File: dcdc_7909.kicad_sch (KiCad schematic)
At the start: 46 parts, among them J1 V_IN, J2 G_IN, J3 RFShield_OnePiece, J4 +10V, J5 G_OUT, J6 -10V, U1 LT3471, U2 LT3045xMSE, U3 LT3094xMSE

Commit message: V2 PCB almost finished.
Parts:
- added C1: 22u, Capacitor_SMD:C_0805_2012Metric_Pad1.18x1.45mm_HandSolder, symbol Device:C_Small
- C10: renamed from C9; footprint Capacitor_SMD:C_1206_3216Metric_Pad1.42x1.75mm_HandSolder -> Capacitor_SMD:C_0805_2012Metric_Pad1.18x1.45mm_HandSolder; LCSC (none) -> C45783
- C11: renamed from C10; footprint Capacitor_SMD:C_0603_1608Metric_Pad1.08x0.95mm_HandSolder -> Capacitor_SMD:C_0603_1608Metric; LCSC (none) -> C57112
- C12: renamed from C11; footprint Capacitor_SMD:C_1206_3216Metric_Pad1.42x1.75mm_HandSolder -> Capacitor_SMD:C_0805_2012Metric_Pad1.18x1.45mm_HandSolder; LCSC (none) -> C15850
- C13: renamed from C12; footprint Capacitor_SMD:C_1206_3216Metric_Pad1.42x1.75mm_HandSolder -> Capacitor_SMD:C_0805_2012Metric_Pad1.18x1.45mm_HandSolder; LCSC (none) -> C15850
- C14: renamed from C13; footprint Capacitor_SMD:C_1206_3216Metric_Pad1.42x1.75mm_HandSolder -> Capacitor_SMD:C_0805_2012Metric_Pad1.18x1.45mm_HandSolder; LCSC (none) -> C15850
- C15: renamed from C14; footprint Capacitor_SMD:C_1206_3216Metric_Pad1.42x1.75mm_HandSolder -> Capacitor_SMD:C_0805_2012Metric_Pad1.18x1.45mm_HandSolder; LCSC (none) -> C15850
- C16: renamed from C15; footprint Capacitor_SMD:C_1206_3216Metric_Pad1.42x1.75mm_HandSolder -> Capacitor_SMD:C_0805_2012Metric_Pad1.18x1.45mm_HandSolder; LCSC (none) -> C15850
- C17: renamed from C16; footprint Capacitor_SMD:C_0603_1608Metric_Pad1.05x0.95mm_HandSolder -> Capacitor_SMD:C_0603_1608Metric; LCSC (none) -> C57112
- C18: renamed from C17; footprint Capacitor_SMD:C_1206_3216Metric_Pad1.42x1.75mm_HandSolder -> Capacitor_SMD:C_0805_2012Metric_Pad1.18x1.45mm_HandSolder; LCSC (none) -> C15850
- C19: renamed from C18; LCSC (none) -> DO NOT POPULATE
- C2: renamed from C1; footprint Capacitor_SMD:C_1206_3216Metric_Pad1.42x1.75mm_HandSolder -> Capacitor_SMD:C_0603_1608Metric; LCSC (none) -> C96446
- C20: renamed from C19; footprint Capacitor_SMD:C_0603_1608Metric_Pad1.05x0.95mm_HandSolder -> Capacitor_SMD:C_0603_1608Metric; LCSC (none) -> C57112
- C21: renamed from C20; LCSC (none) -> DO NOT POPULATE
- C3: renamed from C2; footprint Capacitor_SMD:C_0603_1608Metric_Pad1.08x0.95mm_HandSolder -> Capacitor_SMD:C_0603_1608Metric; LCSC (none) -> C14663
- C4: renamed from C3; footprint Capacitor_SMD:C_0603_1608Metric_Pad1.08x0.95mm_HandSolder -> Capacitor_SMD:C_0603_1608Metric; LCSC (none) -> C1604
- C5: renamed from C4; footprint Capacitor_SMD:C_1206_3216Metric_Pad1.42x1.75mm_HandSolder -> Capacitor_SMD:C_0805_2012Metric_Pad1.18x1.45mm_HandSolder; LCSC (none) -> C45783
- C6: renamed from C5; footprint Capacitor_SMD:C_0603_1608Metric_Pad1.08x0.95mm_HandSolder -> Capacitor_SMD:C_0603_1608Metric; LCSC (none) -> C57112
- C7: renamed from C6; footprint Capacitor_SMD:C_1206_3216Metric_Pad1.42x1.75mm_HandSolder -> Capacitor_SMD:C_0603_1608Metric; LCSC (none) -> C96446
- C8: renamed from C7; footprint Capacitor_SMD:C_1206_3216Metric_Pad1.42x1.75mm_HandSolder -> Capacitor_SMD:C_0603_1608Metric; LCSC (none) -> C96446
- C9: renamed from C8; value 500p -> 470p; footprint Capacitor_SMD:C_0603_1608Metric_Pad1.08x0.95mm_HandSolder -> Capacitor_SMD:C_0603_1608Metric; LCSC (none) -> C1620
- D1, D2: footprint Diode_SMD:D_SOD-323_HandSoldering -> Diode_SMD:D_PowerDI-123; LCSC (none) -> C155287
- D3, D4, J1, J2, J4, J5, J6, TP1, U2, U3: LCSC (none) -> DO NOT POPULATE
- J3: footprint (none) -> RF_Shielding:Laird_Technologies_BMI-S-102_16.50x16.50mm; LCSC (none) -> DO NOT POPULATE
- L1, L2, L3: footprint Inductor_SMD:L_Coilcraft_LPS3010 -> Inductor_SMD:L_Vishay_IHLP-1616; LCSC (none) -> C878322
- R1: footprint Resistor_SMD:R_0603_1608Metric_Pad0.98x0.95mm_HandSolder -> Resistor_SMD:R_0603_1608Metric; LCSC (none) -> C4184
- R2, R3, R4: footprint Resistor_SMD:R_0603_1608Metric_Pad0.98x0.95mm_HandSolder -> Resistor_SMD:R_0603_1608Metric
- R5, R6: footprint Resistor_SMD:R_0603_1608Metric_Pad0.98x0.95mm_HandSolder -> Resistor_SMD:R_0603_1608Metric; LCSC (none) -> C25803
- R7, R8: footprint Resistor_SMD:R_0603_1608Metric_Pad0.98x0.95mm_HandSolder -> Resistor_SMD:R_0603_1608Metric; LCSC (none) -> C21190
- TP2: footprint Diode_SMD:D_SOD-323_HandSoldering -> TestPoint:TestPoint_Pad_D2.0mm; LCSC (none) -> DO NOT POPULATE
- U1: LCSC (none) -> C514422
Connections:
- net GND: now also C1.2
- net VCC: now also C1.1
- no-connect marks 0 -> 3

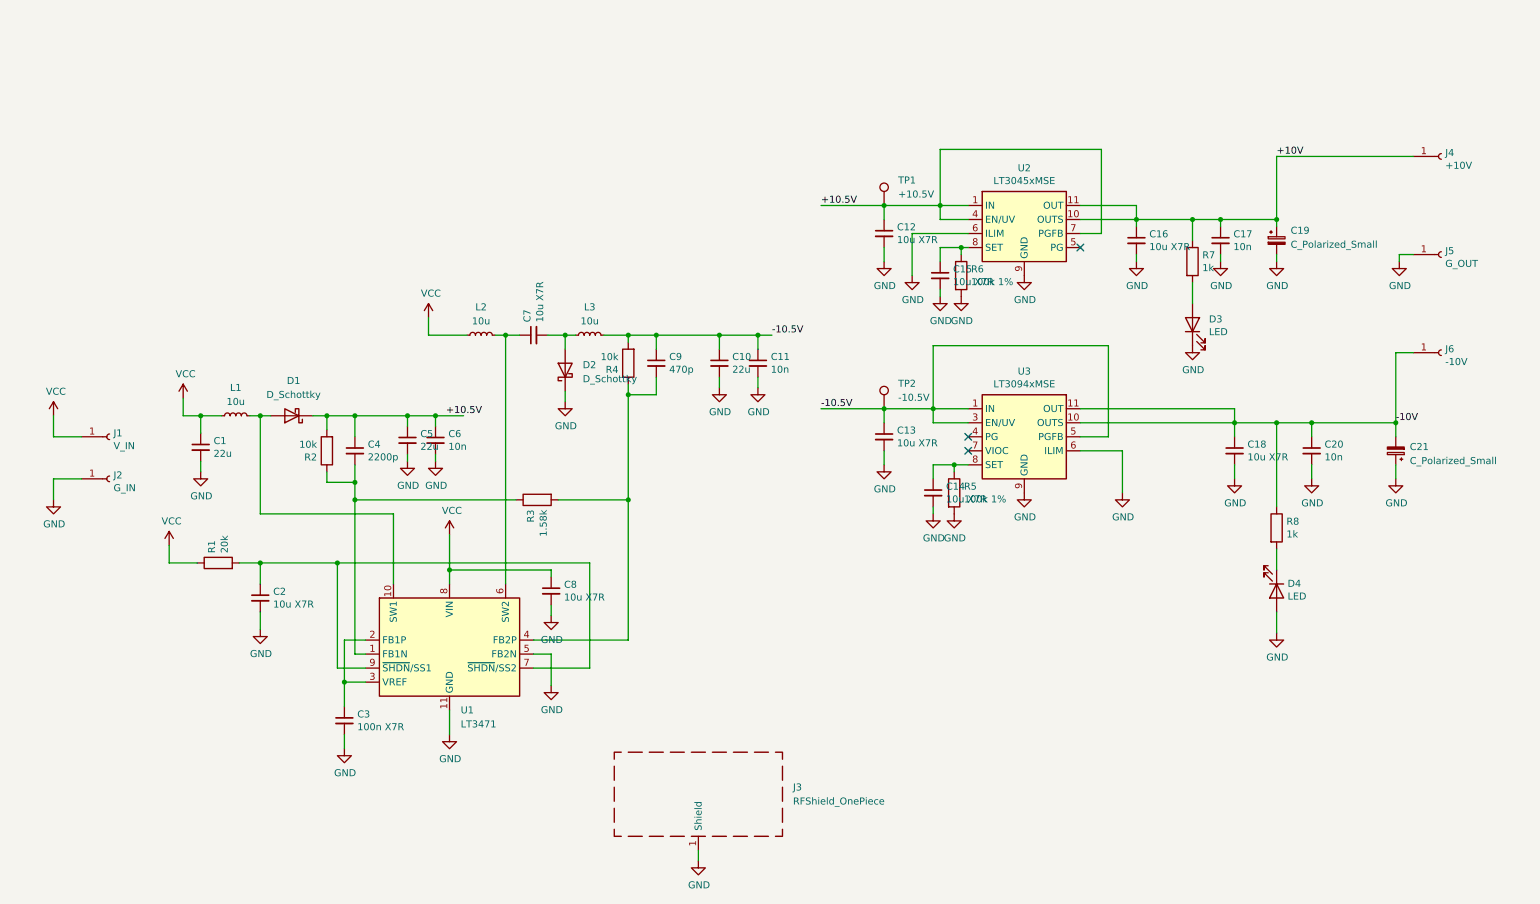
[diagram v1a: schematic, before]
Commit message: One more iteration over the PCB to fit the filtering in the can.
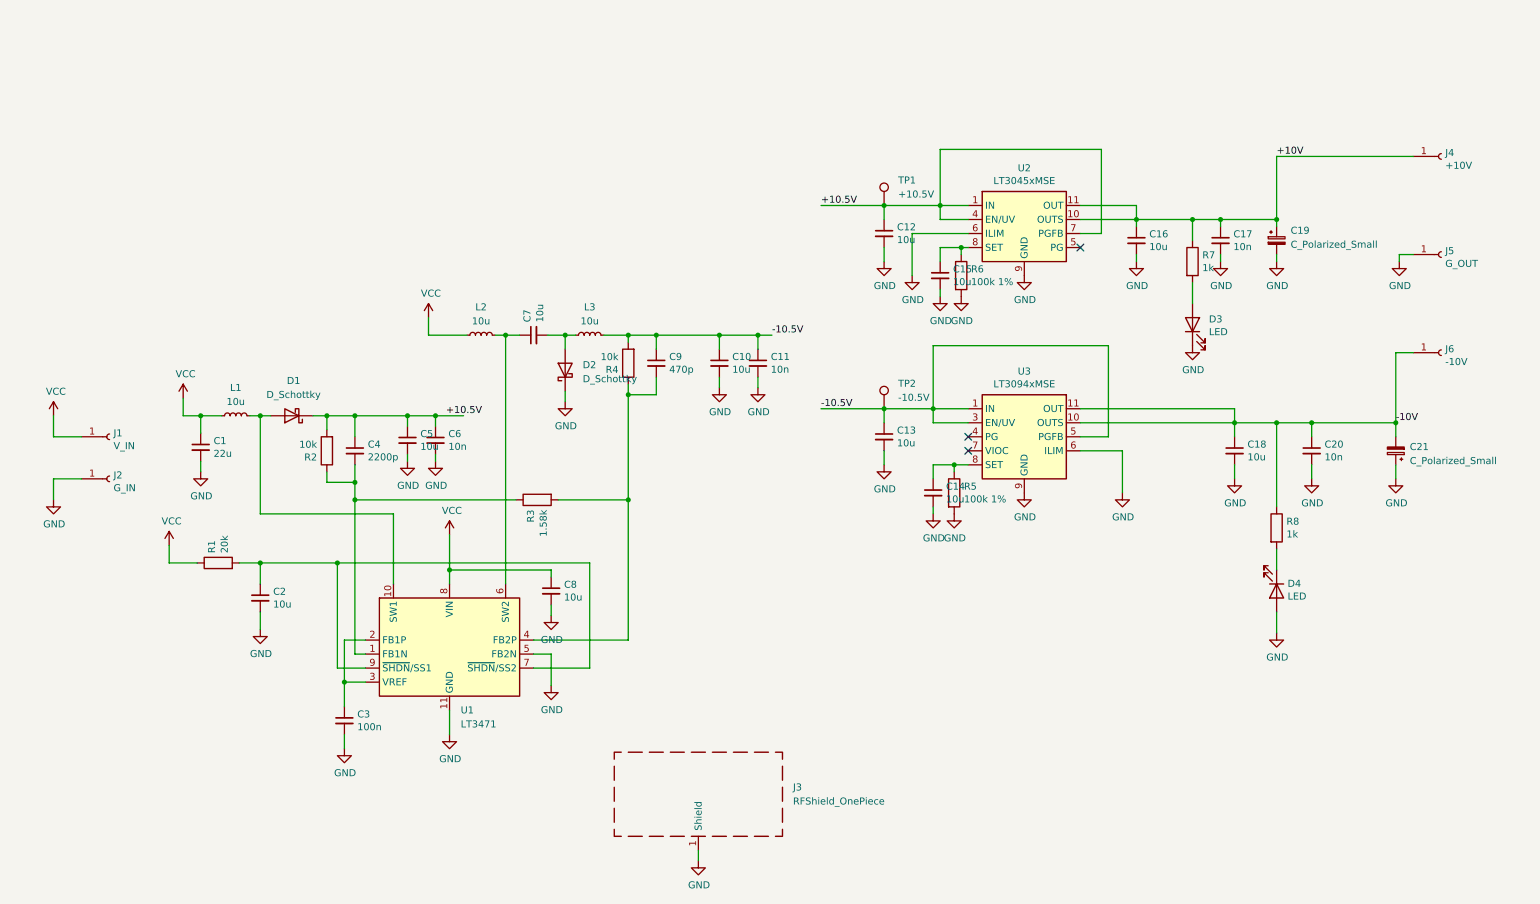
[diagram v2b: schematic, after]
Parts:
- C10, C5: value 22u -> 10u; footprint Capacitor_SMD:C_0805_2012Metric_Pad1.18x1.45mm_HandSolder -> Capacitor_SMD:C_0603_1608Metric; LCSC C45783 -> C96446
- C12, C13, C14, C15, C16, C18, C2, C7, C8: value 10u X7R -> 10u
- C3: value 100n X7R -> 100n
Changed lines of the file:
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@@
       (effects (font (size 1.27 1.27)) (justify left))
     )
-    (property "Value" "10u X7R" (id 1) (at 173.7868 102.108 0)
+    (property "Value" "10u" (id 1) (at 173.7868 102.108 0)
       (effects (font (size 1.27 1.27)) (justify left))
     )
@@
       (effects (font (size 1.27 1.27)) (justify left))
     )
-    (property "Value" "10u X7R" (id 1) (at 173.7868 65.278 0)
+    (property "Value" "10u" (id 1) (at 173.7868 65.278 0)
       (effects (font (size 1.27 1.27)) (justify left))
     )
@@
       (effects (font (size 1.27 1.27)) (justify left))
     )
-    (property "Value" "10u X7R" (id 1) (at 237.2868 104.648 0)
+    (property "Value" "10u" (id 1) (at 237.2868 104.648 0)
       (effects (font (size 1.27 1.27)) (justify left))
     )
@@
       (effects (font (size 1.27 1.27)) (justify left))
     )
-    (property "Value" "10u X7R" (id 1) (at 219.5068 66.548 0)
+    (property "Value" "10u" (id 1) (at 219.5068 66.548 0)
       (effects (font (size 1.27 1.27)) (justify left))
     )
@@
       (effects (font (size 1.27 1.27)) (justify left))
     )
-    (property "Value" "10u X7R" (id 1) (at 182.6768 112.268 0)
+    (property "Value" "10u" (id 1) (at 182.6768 112.268 0)
       (effects (font (size 1.27 1.27)) (justify left))
     )
@@
       (effects (font (size 1.27 1.27)) (justify left))
     )
-    (property "Value" "10u X7R" (id 1) (at 183.9468 72.898 0)
+    (property "Value" "10u" (id 1) (at 183.9468 72.898 0)
       (effects (font (size 1.27 1.27)) (justify left))
     )
@@
       (effects (font (size 1.27 1.27)) (justify left))
     )
-    (property "Value" "100n X7R" (id 1) (at 75.9968 153.543 0)
+    (property "Value" "100n" (id 1) (at 75.9968 153.543 0)
       (effects (font (size 1.27 1.27)) (justify left))
     )
@@
       (effects (font (size 1.27 1.27)) (justify left))
     )
-    (property "Value" "22u" (id 1) (at 143.9418 88.773 0)
-      (effects (font (size 1.27 1.27)) (justify left))
-    )
-    (property "Footprint" "Capacitor_SMD:C_0805_2012Metric_Pad1.18x1.45mm_HandSolder" (id 2) (at 141.605 87.63 0)
+    (property "Value" "10u" (id 1) (at 143.9418 88.773 0)
+      (effects (font (size 1.27 1.27)) (justify left))
+    )
+    (property "Footprint" "Capacitor_SMD:C_0603_1608Metric" (id 2) (at 141.605 87.63 0)
       (effects (font (size 1.27 1.27)) hide)
     )
@@
       (effects (font (size 1.27 1.27)) hide)
     )
-    (property "LCSC" "C45783" (id 4) (at 141.605 87.63 0)
+    (property "LCSC" "C96446" (id 4) (at 141.605 87.63 0)
       (effects (font (size 1.27 1.27)) hide)
     )
@@
       (effects (font (size 1.27 1.27)) (justify left))
     )
-    (property "Value" "22u" (id 1) (at 87.4268 102.743 0)
-      (effects (font (size 1.27 1.27)) (justify left))
-    )
-    (property "Footprint" "Capacitor_SMD:C_0805_2012Metric_Pad1.18x1.45mm_HandSolder" (id 2) (at 85.09 101.6 0)
+    (property "Value" "10u" (id 1) (at 87.4268 102.743 0)
+      (effects (font (size 1.27 1.27)) (justify left))
+    )
+    (property "Footprint" "Capacitor_SMD:C_0603_1608Metric" (id 2) (at 85.09 101.6 0)
       (effects (font (size 1.27 1.27)) hide)
     )
@@
       (effects (font (size 1.27 1.27)) hide)
     )
-    (property "LCSC" "C45783" (id 4) (at 85.09 101.6 0)
+    (property "LCSC" "C96446" (id 4) (at 85.09 101.6 0)
       (effects (font (size 1.27 1.27)) hide)
     )
@@
       (effects (font (size 1.27 1.27)) (justify left))
     )
-    (property "Value" "10u X7R" (id 1) (at 109.093 80.2132 0)
+    (property "Value" "10u" (id 1) (at 109.093 80.2132 0)
       (effects (font (size 1.27 1.27)) (justify left))
     )
@@
       (effects (font (size 1.27 1.27)) (justify left))
     )
-    (property "Value" "10u X7R" (id 1) (at 60.7568 131.318 0)
+    (property "Value" "10u" (id 1) (at 60.7568 131.318 0)
       (effects (font (size 1.27 1.27)) (justify left))
     )
@@
       (effects (font (size 1.27 1.27)) (justify left))
     )
-    (property "Value" "10u X7R" (id 1) (at 113.4618 130.048 0)
+    (property "Value" "10u" (id 1) (at 113.4618 130.048 0)
       (effects (font (size 1.27 1.27)) (justify left))
     )
@@
     )
     (path "/ac7a218e-cc4f-4dc9-b0f0-601a1bec6551"
-      (reference "C2") (unit 1) (value "10u X7R") (footprint "Capacitor_SMD:C_0603_1608Metric")
+      (reference "C2") (unit 1) (value "10u") (footprint "Capacitor_SMD:C_0603_1608Metric")
     )
     (path "/02b992ad-3fbb-4ae9-bf22-6d3f63f2bd4b"
-      (reference "C3") (unit 1) (value "100n X7R") (footprint "Capacitor_SMD:C_0603_1608Metric")
+      (reference "C3") (unit 1) (value "100n") (footprint "Capacitor_SMD:C_0603_1608Metric")
     )
     (path "/efffde45-ed55-4b24-8009-16a95de1f75d"
@@
     )
     (path "/33c03a2e-c7c0-4ac0-8b58-0f5daee7b249"
-      (reference "C5") (unit 1) (value "22u") (footprint "Capacitor_SMD:C_0805_2012Metric_Pad1.18x1.45mm_HandSolder")
+      (reference "C5") (unit 1) (value "10u") (footprint "Capacitor_SMD:C_0603_1608Metric")
     )
     (path "/6fd76ca0-0509-4b7d-b0ea-a6ae521f886a"
@@
     )
     (path "/9d2e0a36-c9c2-4149-ab8c-dbef005320d9"
-      (reference "C7") (unit 1) (value "10u X7R") (footprint "Capacitor_SMD:C_0603_1608Metric")
+      (reference "C7") (unit 1) (value "10u") (footprint "Capacitor_SMD:C_0603_1608Metric")
     )
     (path "/f2d832c7-f451-482a-b361-65585b8b26a2"
-      (reference "C8") (unit 1) (value "10u X7R") (footprint "Capacitor_SMD:C_0603_1608Metric")
+      (reference "C8") (unit 1) (value "10u") (footprint "Capacitor_SMD:C_0603_1608Metric")
     )
     (path "/6e0ed22c-ecdc-40a8-afb4-ac6ef4db0660"
@@
     )
     (path "/0703d55f-cdae-441a-870f-e2fd578f5c07"
-      (reference "C10") (unit 1) (value "22u") (footprint "Capacitor_SMD:C_0805_2012Metric_Pad1.18x1.45mm_HandSolder")
+      (reference "C10") (unit 1) (value "10u") (footprint "Capacitor_SMD:C_0603_1608Metric")
     )
     (path "/81a36db3-9b5f-4cf3-83b8-c8c8ac5701dd"
@@
     )
     (path "/00000000-0000-0000-0000-00005ea08d58"
-      (reference "C12") (unit 1) (value "10u X7R") (footprint "Capacitor_SMD:C_0805_2012Metric_Pad1.18x1.45mm_HandSolder")
+      (reference "C12") (unit 1) (value "10u") (footprint "Capacitor_SMD:C_0805_2012Metric_Pad1.18x1.45mm_HandSolder")
     )
     (path "/00000000-0000-0000-0000-00005ea08764"
-      (reference "C13") (unit 1) (value "10u X7R") (footprint "Capacitor_SMD:C_0805_2012Metric_Pad1.18x1.45mm_HandSolder")
+      (reference "C13") (unit 1) (value "10u") (footprint "Capacitor_SMD:C_0805_2012Metric_Pad1.18x1.45mm_HandSolder")
     )
     (path "/00000000-0000-0000-0000-00005ea20b33"
-      (reference "C14") (unit 1) (value "10u X7R") (footprint "Capacitor_SMD:C_0805_2012Metric_Pad1.18x1.45mm_HandSolder")
+      (reference "C14") (unit 1) (value "10u") (footprint "Capacitor_SMD:C_0805_2012Metric_Pad1.18x1.45mm_HandSolder")
     )
     (path "/00000000-0000-0000-0000-00005ea22de1"
-      (reference "C15") (unit 1) (value "10u X7R") (footprint "Capacitor_SMD:C_0805_2012Metric_Pad1.18x1.45mm_HandSolder")
+      (reference "C15") (unit 1) (value "10u") (footprint "Capacitor_SMD:C_0805_2012Metric_Pad1.18x1.45mm_HandSolder")
     )
     (path "/00000000-0000-0000-0000-00005ea1a7bc"
-      (reference "C16") (unit 1) (value "10u X7R") (footprint "Capacitor_SMD:C_0805_2012Metric_Pad1.18x1.45mm_HandSolder")
+      (reference "C16") (unit 1) (value "10u") (footprint "Capacitor_SMD:C_0805_2012Metric_Pad1.18x1.45mm_HandSolder")
     )
     (path "/00000000-0000-0000-0000-00005ea255d5"
@@
     )
     (path "/00000000-0000-0000-0000-00005ea1a1dc"
-      (reference "C18") (unit 1) (value "10u X7R") (footprint "Capacitor_SMD:C_0805_2012Metric_Pad1.18x1.45mm_HandSolder")
+      (reference "C18") (unit 1) (value "10u") (footprint "Capacitor_SMD:C_0805_2012Metric_Pad1.18x1.45mm_HandSolder")
     )
     (path "/5afc8212-c351-4768-9cd3-90ba43642e5a"

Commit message: Updated ground fill zones.
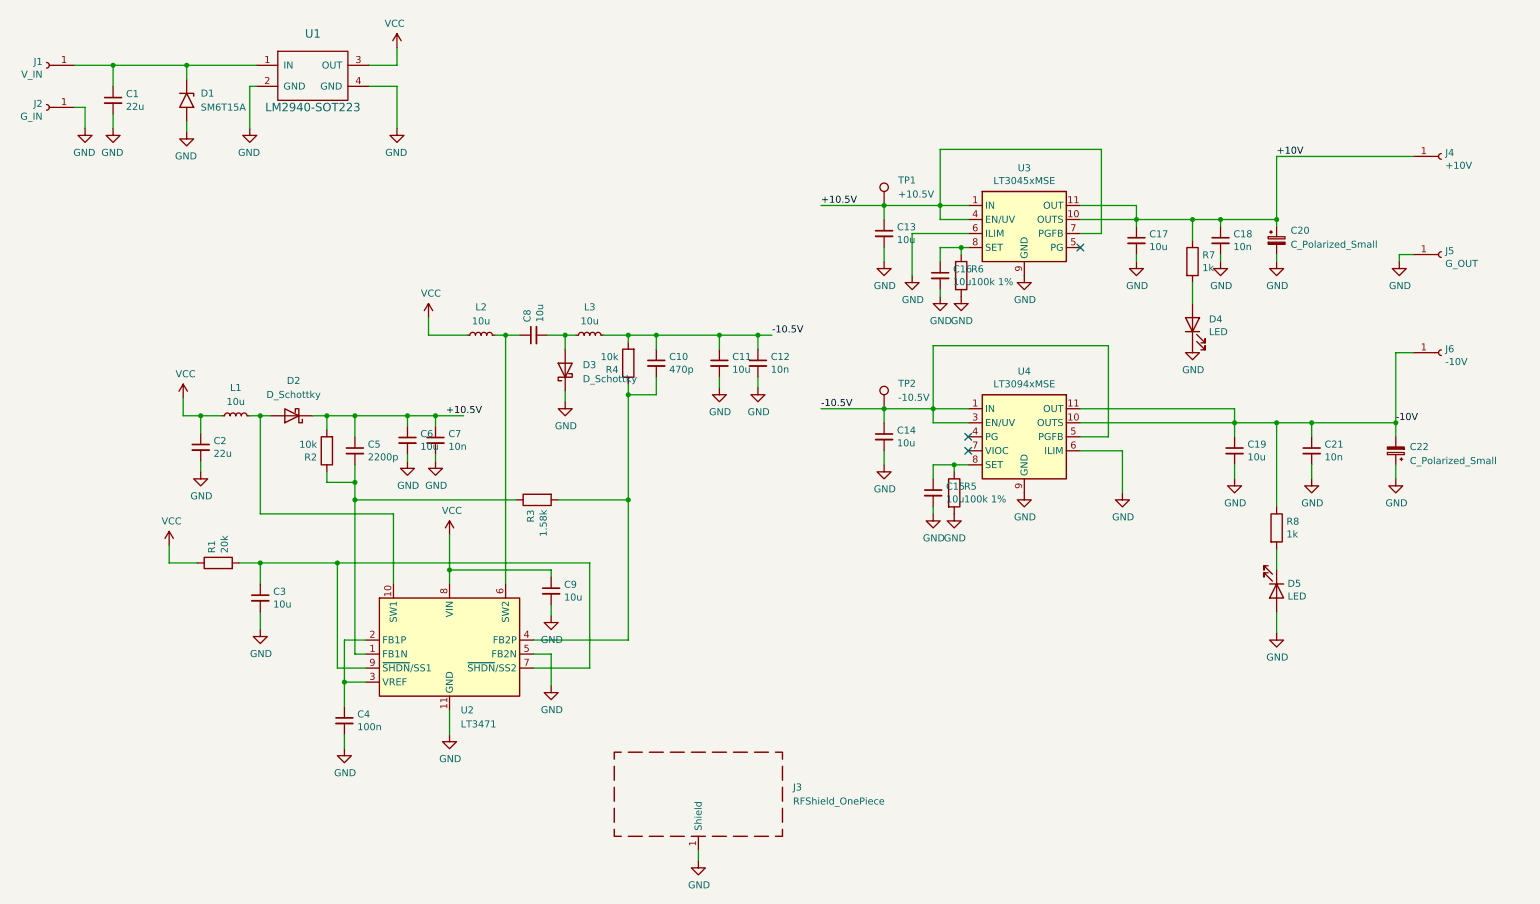
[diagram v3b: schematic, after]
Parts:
- added C1: 22u, Capacitor_SMD:C_0805_2012Metric_Pad1.18x1.45mm_HandSolder, symbol Device:C_Small
- added D1: SM6T15A, Diode_SMD:D_SMB, symbol Diode:SM6T15A
- added U1: LM2940-SOT223, Package_TO_SOT_SMD:SOT-223, symbol marcin_library:LM2940-SOT223
- renumbered C9 to C10, C10 to C11, C11 to C12, C12 to C13, C13 to C14, C14 to C15, C15 to C16, C16 to C17, C17 to C18, C18 to C19, C1 to C2, C19 to C20, C20 to C21, C21 to C22, C2 to C3, C3 to C4, C4 to C5, C5 to C6, C6 to C7, C7 to C8, C8 to C9, D1 to D2, D2 to D3, D3 to D4, D4 to D5, U1 to U2, U2 to U3, U3 to U4
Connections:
- net GND: now also C1.2, D1.2 (A2), U1.2 (GND), U1.4 (GND)
- net VCC: now also U1.3 (OUT); no longer J1.1 (Pin_1)
- new net: C1.1, D1.1 (A1), J1.1 (Pin_1), U1.1 (IN)
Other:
- moved on the sheet: J1, J2
